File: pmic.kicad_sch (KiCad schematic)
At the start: 19 parts, among them Q2 PMOS, SW2 PWR_BTN, U1 NPM1300-CAAA-R

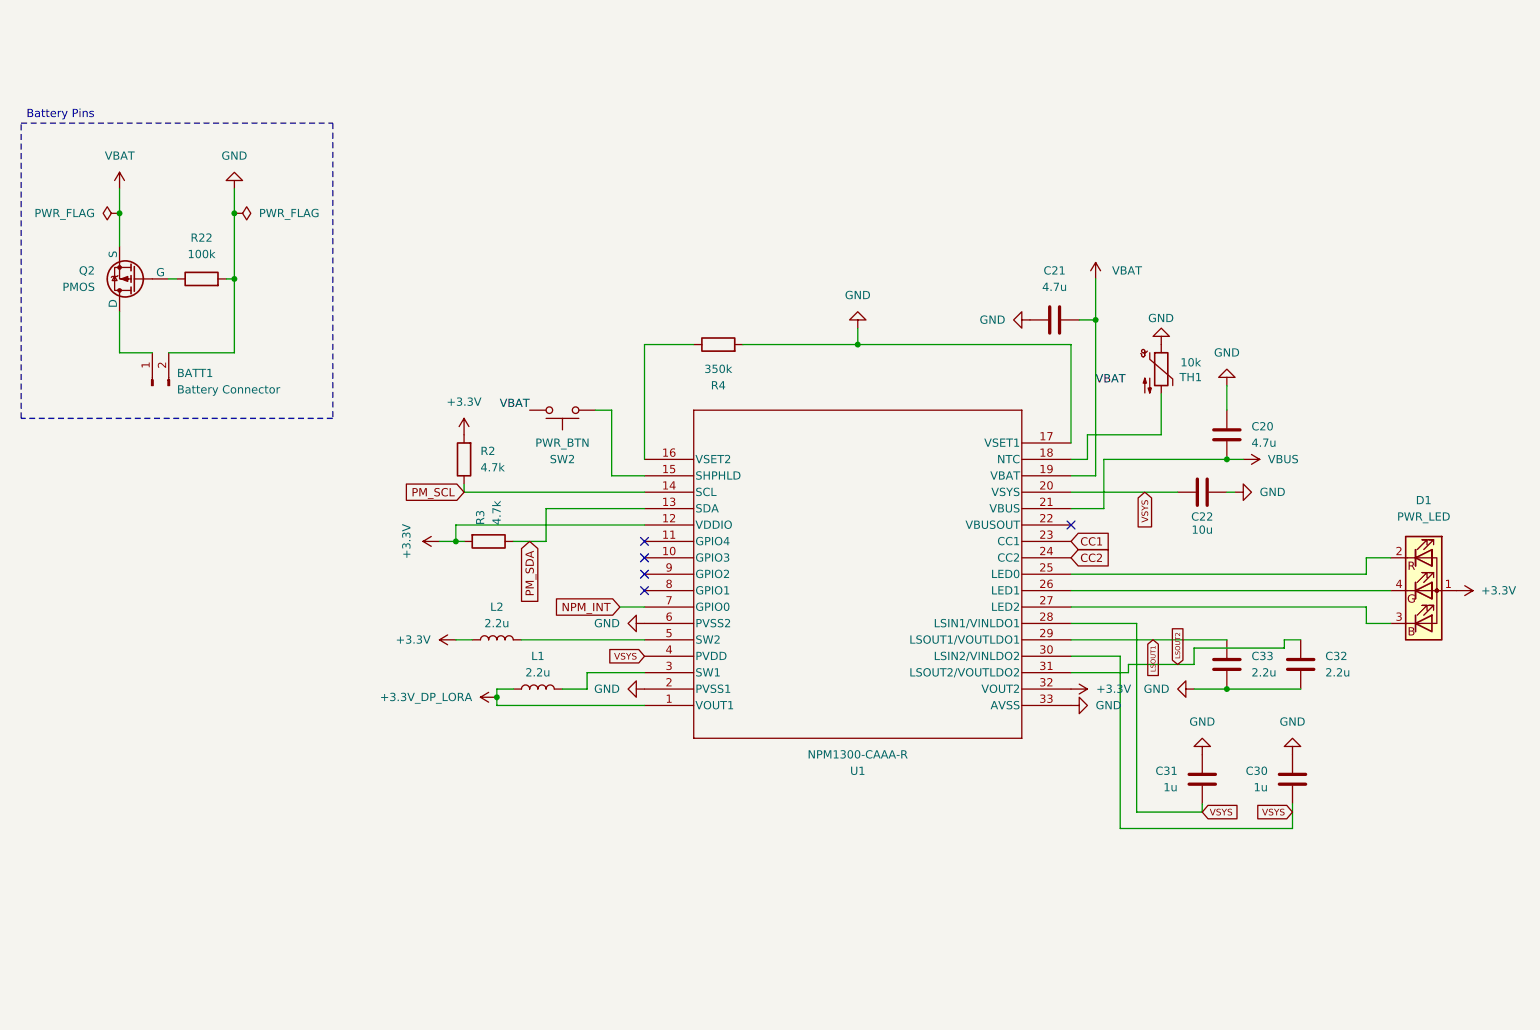
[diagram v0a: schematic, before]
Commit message: Updated with new power rails, added sensors and gps symbol
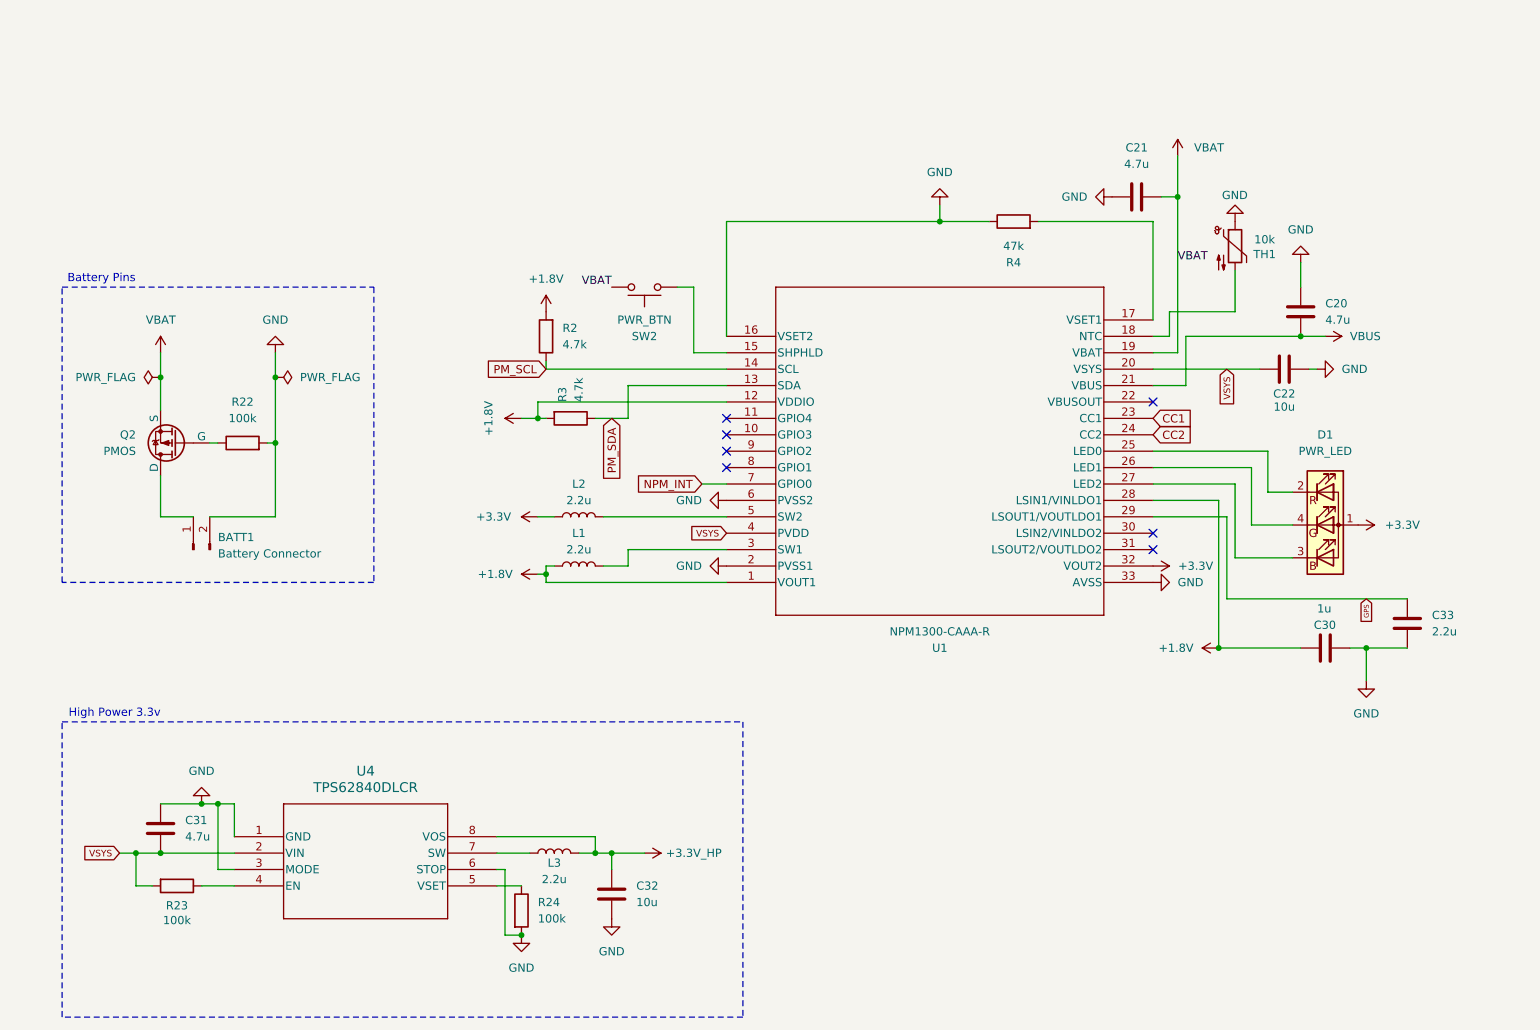
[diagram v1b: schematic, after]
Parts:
- added L3: 2.2u, symbol Device:L
- added R23, R24: 100k, symbol Device:R
- added U4: TPS62840DLCR, VSON8_2P1X1P6_TEX, symbol TheSummitProject:TPS62840DLCR
- C31: value 1u -> 4.7u; footprint Capacitor_SMD:C_0603_1608Metric -> (none)
- C32: value 2.2u -> 10u; footprint Capacitor_SMD:C_0603_1608Metric -> (none)
- R4: value 350k -> 47k
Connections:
- net +3.3V: no longer R2.2, R3.2, U1.12 (VDDIO)
- net GND: now also C32.2, R4.1, U1.16 (VSET2), R24.2, U4.1 (GND), U4.3 (MODE), U4.6 (STOP); no longer C32.1, R4.2, U1.17 (VSET1)
- net VSYS: now also R23.2, U4.2 (VIN); no longer C30.2, U1.28 (LSIN1/VINLDO1), U1.30 (LSIN2/VINLDO2)
- net +3.3V_DP_LORA renamed +1.8V
- net +1.8V: now also C30.2, R2.2, R3.2, U1.12 (VDDIO), U1.28 (LSIN1/VINLDO1)
- net LSOUT1 renamed GPS
- net LSOUT2: no longer names the net of U1.31 (LSOUT2/VOUTLDO2)
- net LSOUT2: no longer C32.2
- new net: R23.1, U4.4 (EN)
- new net: R24.1, U4.5 (VSET)
- new net: L3.1, U4.7 (SW)
- new net: R4.2, U1.17 (VSET1)
- new net +3.3V_HP: C32.1, L3.2, U4.8 (VOS)
- no-connect marks 5 -> 7
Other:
- note added: "High Power 3.3v"
- moved on the sheet: BATT1, C20, C21, C22, D1, L1, L2, Q2, R2, R22, R3, SW2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

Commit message: added mux for usb, cleaned up schematic for pcb design, setup new pcb with correct size
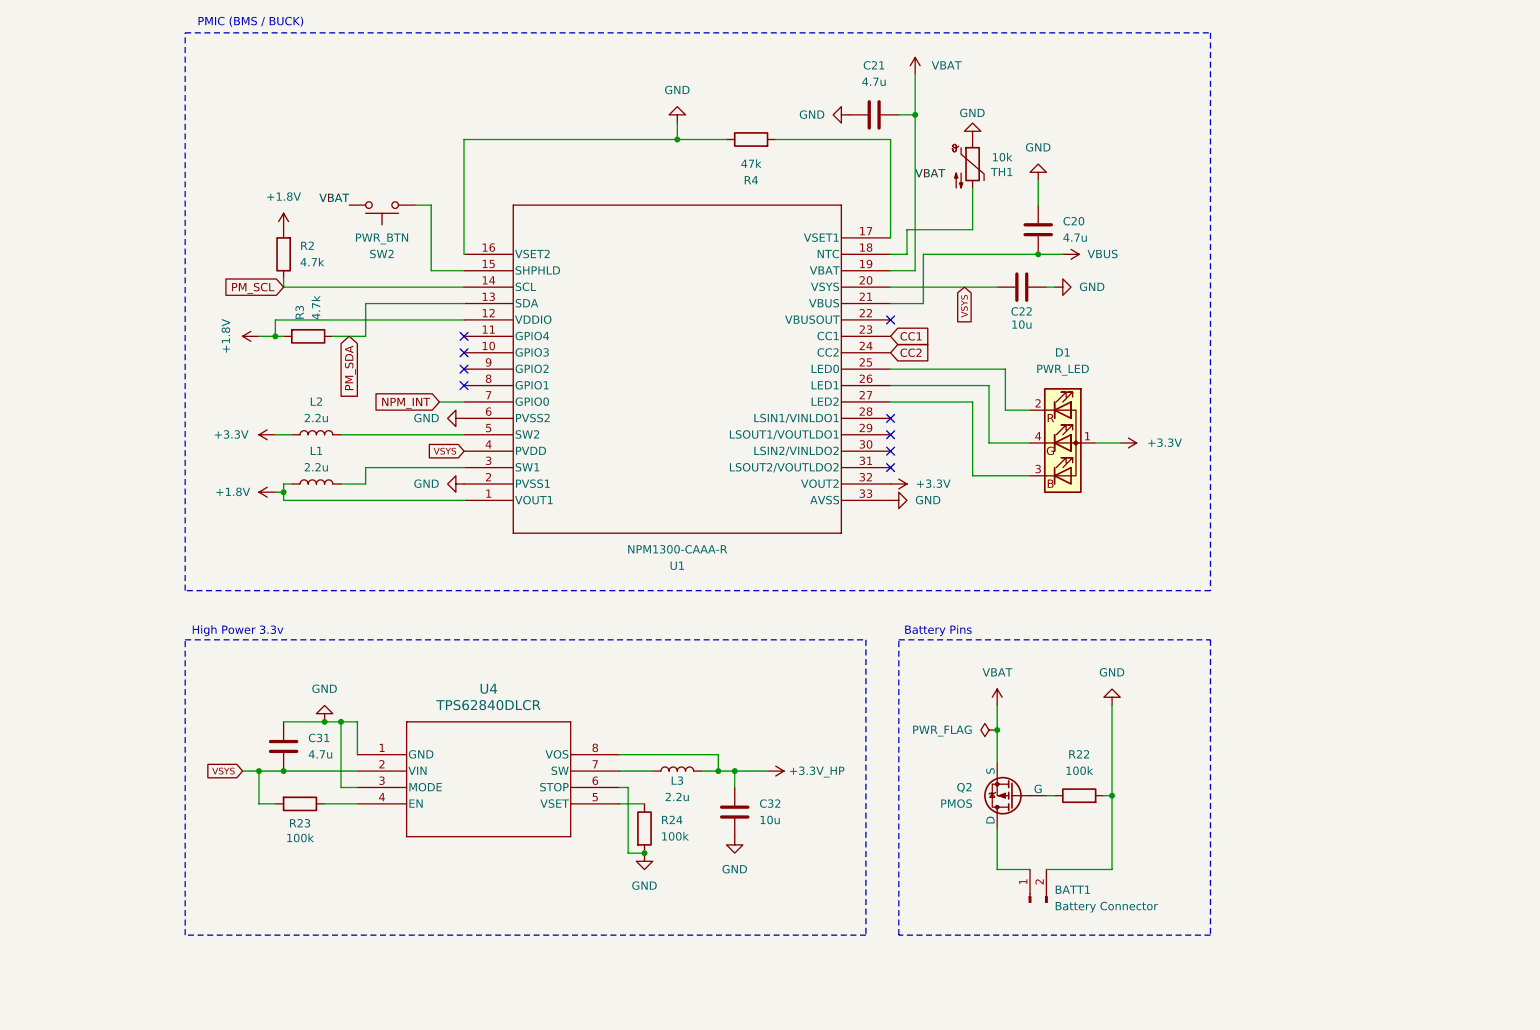
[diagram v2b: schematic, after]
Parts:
- removed C30: 1u, Capacitor_SMD:C_0603_1608Metric, symbol Device:C
- removed C33: 2.2u, Capacitor_SMD:C_0603_1608Metric, symbol Device:C
- BATT1: footprint Connector_PinHeader_2.54mm:PinHeader_1x02_P2.54mm_Vertical -> Connector_PinHeader_2.54mm:PinHeader_1x02_P2.54mm_Horizontal
- C31, C32: footprint (none) -> Capacitor_SMD:C_0805_2012Metric
- L3: footprint (none) -> Inductor_SMD:L_0805_2012Metric
- Q2: footprint (none) -> Package_TO_SOT_SMD:SOT-23
- R22, R23, R24: footprint (none) -> Resistor_SMD:R_0603_1608Metric
- U4: footprint VSON8_2P1X1P6_TEX -> TheSummitProject:VSON8_2P1X1P6_TEX
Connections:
- net +1.8V: no longer U1.28 (LSIN1/VINLDO1)
- net GPS: no longer names the net of U1.29 (LSOUT1/VOUTLDO1)
- no-connect marks 7 -> 9
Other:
- note added: "PMIC (BMS / BUCK)"
- moved on the sheet: BATT1, C20, C21, C22, C31, C32, D1, L1, L2, L3, Q2, R2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
